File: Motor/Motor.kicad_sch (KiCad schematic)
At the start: 5 parts, among them J1 Screw_Terminal_01x04, U2 DRV8833RTY

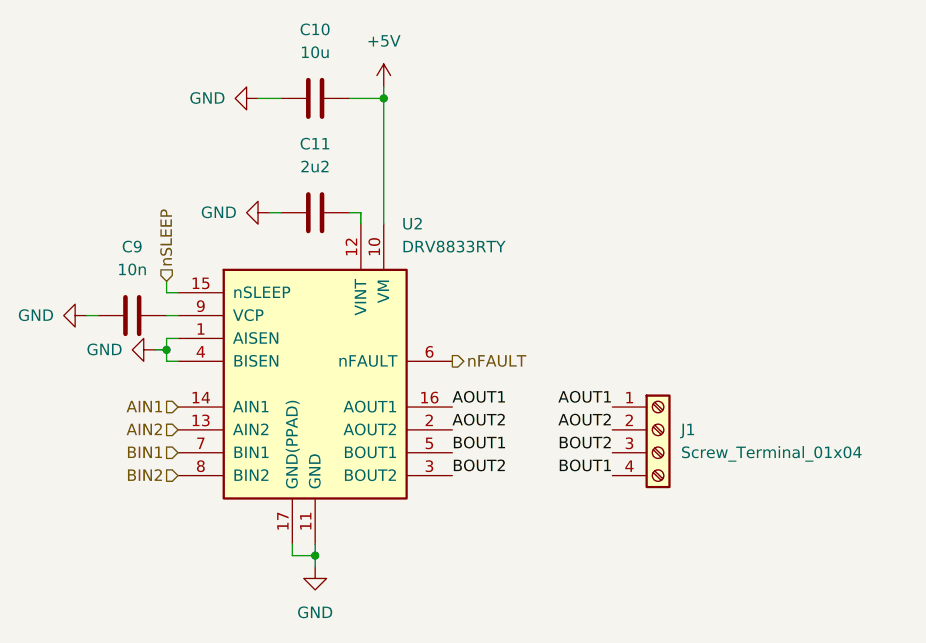
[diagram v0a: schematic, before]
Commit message: First week after winter break. Changed Power circuit design to use different DC to DC converter Setting correct footprints for the components like resistors and capacitors.
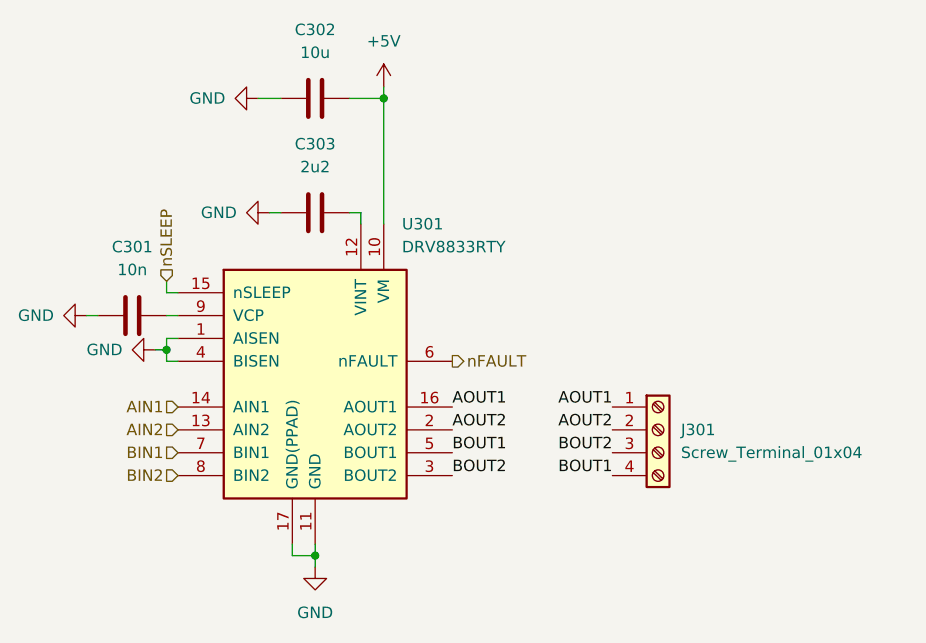
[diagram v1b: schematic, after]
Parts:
- C301: renamed from C9; footprint Capacitor_SMD:C_0201_0603Metric -> Capacitor_SMD:C_0805_2012Metric; Manufacturer_Name (none) -> Samsung Electro-Mechanics; Manufacturer_Part_Number (none) -> CL21B103KBANNNC
- C302: renamed from C10; footprint Capacitor_SMD:C_0201_0603Metric -> Capacitor_SMD:C_0603_1608Metric; Manufacturer_Name (none) -> Samsung Electro-Mechanics; Manufacturer_Part_Number (none) -> CL10A106KP8NNNC
- C303: renamed from C11; footprint Capacitor_SMD:C_0201_0603Metric -> Capacitor_SMD:C_0603_1608Metric; Manufacturer_Name (none) -> Samsung Electro-Mechanics; Manufacturer_Part_Number (none) -> CL10A225KO8NNNC
- renumbered J1 to J301, U2 to U301
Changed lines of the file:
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@@
   (symbol (lib_id "Device:C") (at 82.55 59.69 90) (unit 1)
     (in_bom yes) (on_board yes) (fields_autoplaced)
-    (property "Reference" "C9" (id 0) (at 82.55 52.07 90))
+    (property "Reference" "C301" (id 0) (at 82.55 52.07 90))
     (property "Value" "10n" (id 1) (at 82.55 54.61 90))
-    (property "Footprint" "Capacitor_SMD:C_0201_0603Metric" (id 2) (at 86.36 58.7248 0)
+    (property "Footprint" "Capacitor_SMD:C_0805_2012Metric" (id 2) (at 86.36 58.7248 0)
       (effects (font (size 1.27 1.27)) hide)
     )
     (property "Datasheet" "~" (id 3) (at 82.55 59.69 0)
+      (effects (font (size 1.27 1.27)) hide)
+    )
+    (property "Manufacturer_Name" "Samsung Electro-Mechanics" (id 4) (at 82.55 59.69 0)
+      (effects (font (size 1.27 1.27)) hide)
+    )
+    (property "Manufacturer_Part_Number" "CL21B103KBANNNC" (id 5) (at 82.55 59.69 0)
       (effects (font (size 1.27 1.27)) hide)
     )
@@
   (symbol (lib_id "Device:C") (at 102.87 35.56 90) (unit 1)
     (in_bom yes) (on_board yes) (fields_autoplaced)
-    (property "Reference" "C10" (id 0) (at 102.87 27.94 90))
+    (property "Reference" "C302" (id 0) (at 102.87 27.94 90))
     (property "Value" "10u" (id 1) (at 102.87 30.48 90))
-    (property "Footprint" "Capacitor_SMD:C_0201_0603Metric" (id 2) (at 106.68 34.5948 0)
+    (property "Footprint" "Capacitor_SMD:C_0603_1608Metric" (id 2) (at 106.68 34.5948 0)
       (effects (font (size 1.27 1.27)) hide)
     )
     (property "Datasheet" "~" (id 3) (at 102.87 35.56 0)
+      (effects (font (size 1.27 1.27)) hide)
+    )
+    (property "Manufacturer_Name" "Samsung Electro-Mechanics" (id 4) (at 102.87 35.56 0)
+      (effects (font (size 1.27 1.27)) hide)
+    )
+    (property "Manufacturer_Part_Number" "CL10A106KP8NNNC" (id 5) (at 102.87 35.56 0)
       (effects (font (size 1.27 1.27)) hide)
     )
@@
   (symbol (lib_id "power:GND") (at 97.79 48.26 270) (unit 1)
     (in_bom yes) (on_board yes)
-    (property "Reference" "#PWR0113" (id 0) (at 91.44 48.26 0)
+    (property "Reference" "#PWR0304" (id 0) (at 91.44 48.26 0)
       (effects (font (size 1.27 1.27)) hide)
     )
@@
   (symbol (lib_id "power:GND") (at 102.87 87.63 0) (unit 1)
     (in_bom yes) (on_board yes) (fields_autoplaced)
-    (property "Reference" "#PWR0110" (id 0) (at 102.87 93.98 0)
+    (property "Reference" "#PWR0305" (id 0) (at 102.87 93.98 0)
       (effects (font (size 1.27 1.27)) hide)
     )
@@
   (symbol (lib_id "Driver_Motor:DRV8833RTY") (at 102.87 67.31 0) (unit 1)
     (in_bom yes) (on_board yes) (fields_autoplaced)
-    (property "Reference" "U2" (id 0) (at 112.5094 49.53 0)
+    (property "Reference" "U301" (id 0) (at 112.5094 49.53 0)
       (effects (font (size 1.27 1.27)) (justify left))
     )
@@
   (symbol (lib_id "Connector:Screw_Terminal_01x04") (at 140.97 72.39 0) (unit 1)
     (in_bom yes) (on_board yes) (fields_autoplaced)
-    (property "Reference" "J1" (id 0) (at 143.51 72.3899 0)
+    (property "Reference" "J301" (id 0) (at 143.51 72.3899 0)
       (effects (font (size 1.27 1.27)) (justify left))
     )
@@
   (symbol (lib_id "power:GND") (at 85.09 63.5 270) (unit 1)
     (in_bom yes) (on_board yes)
-    (property "Reference" "#PWR0115" (id 0) (at 78.74 63.5 0)
+    (property "Reference" "#PWR0302" (id 0) (at 78.74 63.5 0)
       (effects (font (size 1.27 1.27)) hide)
     )
@@
   (symbol (lib_id "power:GND") (at 77.47 59.69 270) (unit 1)
     (in_bom yes) (on_board yes)
-    (property "Reference" "#PWR0114" (id 0) (at 71.12 59.69 0)
+    (property "Reference" "#PWR0301" (id 0) (at 71.12 59.69 0)
       (effects (font (size 1.27 1.27)) hide)
     )
@@
   (symbol (lib_id "Device:C") (at 102.87 48.26 90) (unit 1)
     (in_bom yes) (on_board yes) (fields_autoplaced)
-    (property "Reference" "C11" (id 0) (at 102.87 40.64 90))
+    (property "Reference" "C303" (id 0) (at 102.87 40.64 90))
     (property "Value" "2u2" (id 1) (at 102.87 43.18 90))
-    (property "Footprint" "Capacitor_SMD:C_0201_0603Metric" (id 2) (at 106.68 47.2948 0)
+    (property "Footprint" "Capacitor_SMD:C_0603_1608Metric" (id 2) (at 106.68 47.2948 0)
       (effects (font (size 1.27 1.27)) hide)
     )
     (property "Datasheet" "~" (id 3) (at 102.87 48.26 0)
+      (effects (font (size 1.27 1.27)) hide)
+    )
+    (property "Manufacturer_Name" "Samsung Electro-Mechanics" (id 4) (at 102.87 48.26 0)
+      (effects (font (size 1.27 1.27)) hide)
+    )
+    (property "Manufacturer_Part_Number" "CL10A225KO8NNNC" (id 5) (at 102.87 48.26 0)
       (effects (font (size 1.27 1.27)) hide)
     )
@@
   (symbol (lib_id "power:+5V") (at 110.49 34.29 0) (unit 1)
     (in_bom yes) (on_board yes) (fields_autoplaced)
-    (property "Reference" "#PWR0111" (id 0) (at 110.49 38.1 0)
+    (property "Reference" "#PWR0306" (id 0) (at 110.49 38.1 0)
       (effects (font (size 1.27 1.27)) hide)
     )
@@
   (symbol (lib_id "power:GND") (at 96.52 35.56 270) (unit 1)
     (in_bom yes) (on_board yes)
-    (property "Reference" "#PWR0112" (id 0) (at 90.17 35.56 0)
+    (property "Reference" "#PWR0303" (id 0) (at 90.17 35.56 0)
       (effects (font (size 1.27 1.27)) hide)
     )

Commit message: Weekend progress
Things that remain:
4 LEDs to Microcontroller
7-Seg to Microcontroller
LCD to Microcontroller
Microphone and Speakers to Microcontroller
Power circuitry
USB-C connector
Reset and Boot buttons
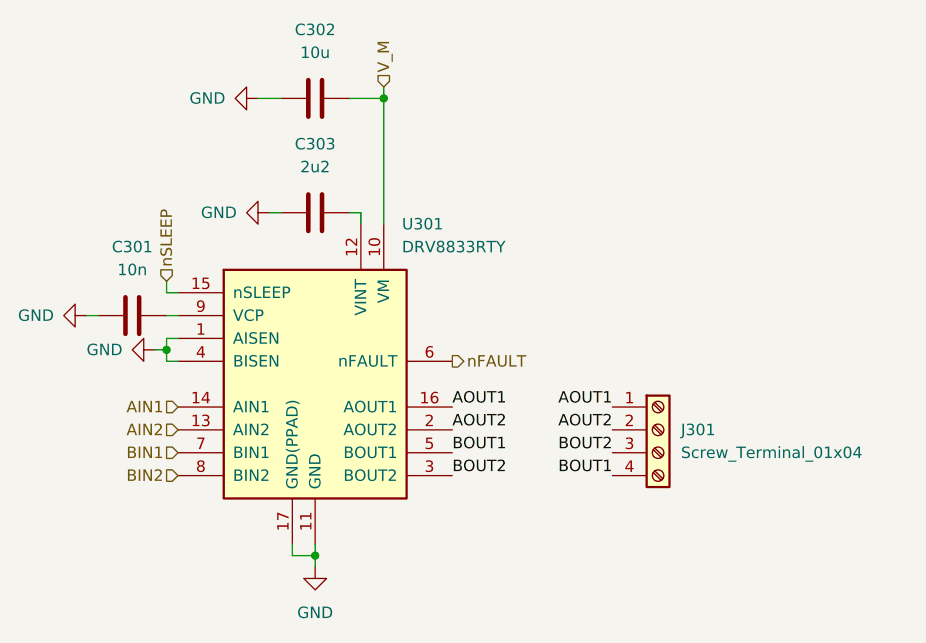
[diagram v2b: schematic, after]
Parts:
- C301: footprint Capacitor_SMD:C_0805_2012Metric -> Capacitor_SMD:C_0603_1608Metric; Manufacturer_Part_Number CL21B103KBANNNC -> 0603B103K500NT
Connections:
- net +5V renamed V_M
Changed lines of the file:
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@@
     (effects (font (size 1.27 1.27)) (justify right))
+  )
+  (hierarchical_label "V_M" (shape input) (at 110.49 34.29 90)
+    (effects (font (size 1.27 1.27)) (justify left))
   )
   (hierarchical_label "AIN2" (shape input) (at 87.63 72.39 180)
@@
     (property "Reference" "C301" (id 0) (at 82.55 52.07 90))
     (property "Value" "10n" (id 1) (at 82.55 54.61 90))
-    (property "Footprint" "Capacitor_SMD:C_0805_2012Metric" (id 2) (at 86.36 58.7248 0)
+    (property "Footprint" "Capacitor_SMD:C_0603_1608Metric" (id 2) (at 86.36 58.7248 0)
       (effects (font (size 1.27 1.27)) hide)
     )
@@
       (effects (font (size 1.27 1.27)) hide)
     )
-    (property "Manufacturer_Part_Number" "CL21B103KBANNNC" (id 5) (at 82.55 59.69 0)
+    (property "Manufacturer_Part_Number" "0603B103K500NT" (id 5) (at 82.55 59.69 0)
       (effects (font (size 1.27 1.27)) hide)
     )
@@
     (pin "2")
   )
-  (symbol (lib_id "power:+5V") (at 110.49 34.29 0) (unit 1)
-    (in_bom yes) (on_board yes) (fields_autoplaced)
-    (property "Reference" "#PWR0306" (id 0) (at 110.49 38.1 0)
-      (effects (font (size 1.27 1.27)) hide)
-    )
-    (property "Value" "+5V" (id 1) (at 110.49 29.21 0))
-    (property "Footprint" "" (id 2) (at 110.49 34.29 0)
-      (effects (font (size 1.27 1.27)) hide)
-    )
-    (property "Datasheet" "" (id 3) (at 110.49 34.29 0)
-      (effects (font (size 1.27 1.27)) hide)
-    )
-    (pin "1")
-  )
   (symbol (lib_id "power:GND") (at 96.52 35.56 270) (unit 1)

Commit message: Update BOM and POC files
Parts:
- U301: Manufacturer_Name (none) -> Texas Instruments; Manufacturer_Part_Number (none) -> DRV8833RTYT
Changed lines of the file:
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@@
+      (effects (font (size 1.27 1.27)) hide)
+    )
+    (property "Manufacturer_Name" "Texas Instruments" (id 4) (at 102.87 67.31 0)
+      (effects (font (size 1.27 1.27)) hide)
+    )
+    (property "Manufacturer_Part_Number" "DRV8833RTYT" (id 5) (at 102.87 67.31 0)
       (effects (font (size 1.27 1.27)) hide)
     )
